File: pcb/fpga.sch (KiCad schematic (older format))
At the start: 29 parts, among them J1 CONN_INTEGRALSTICK_FPGA_DEVICE, Q1 SSM6N58NU, Q2 SSM6N58NU, Q3 SSM6N58NU, U12 DSC6001HI2A-025.0000‎, U2 XC7A50T-1FTG256C, U9 AT24MAC402-UDFN

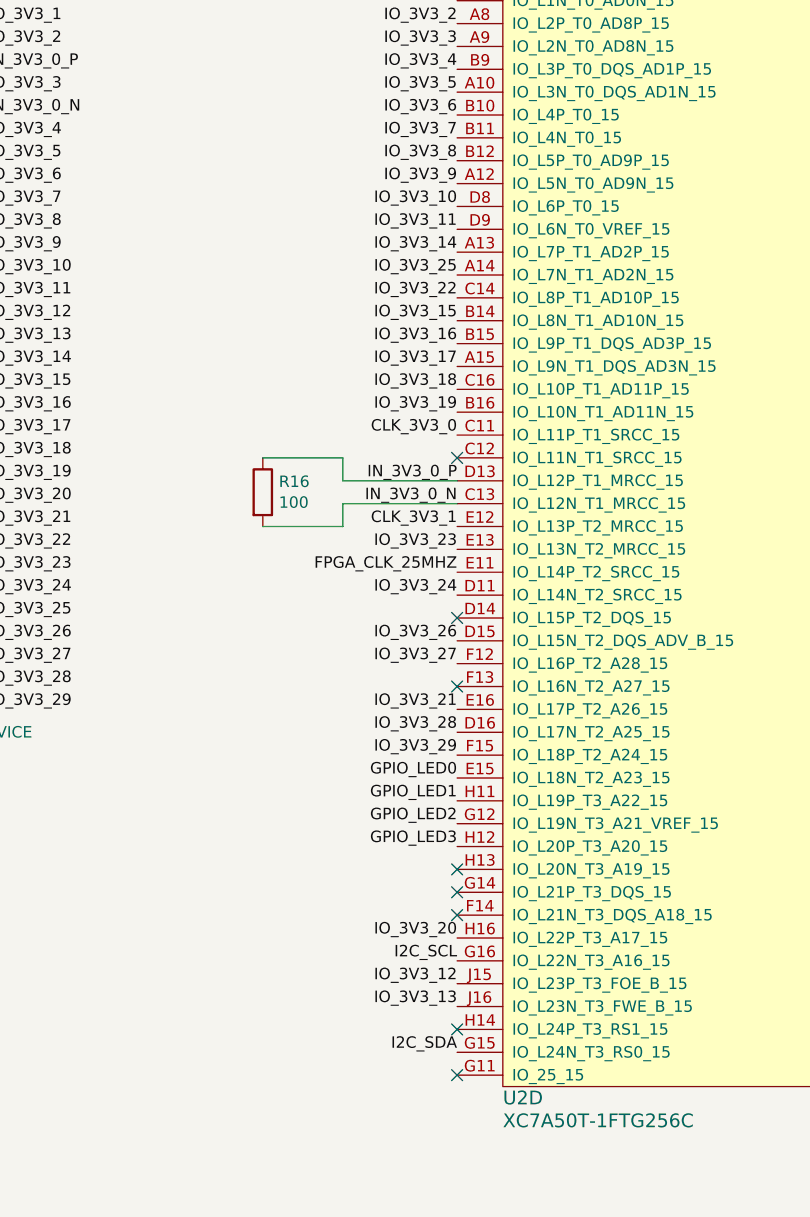
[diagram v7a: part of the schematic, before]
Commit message: Lots more routing of 3.3V GPIO bus
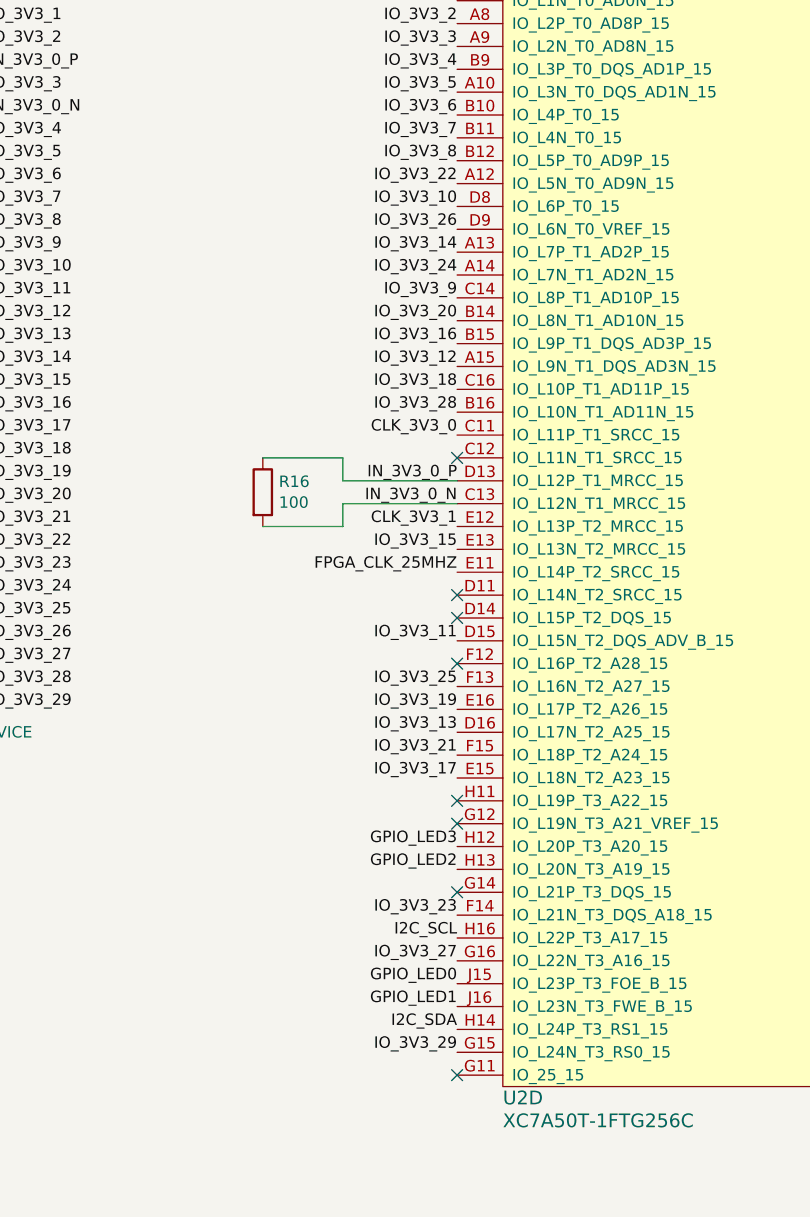
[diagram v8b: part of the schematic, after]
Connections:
- net GPIO_LED0: now also U2.J15 (IO_L23P_T3_FOE_B_15); no longer U2.E15 (IO_L18N_T2_A23_15)
- net GPIO_LED1: now also U2.J16 (IO_L23N_T3_FWE_B_15); no longer U2.H11 (IO_L19P_T3_A22_15)
- net GPIO_LED2: now also U2.H13 (IO_L20N_T3_A19_15); no longer U2.G12 (IO_L19N_T3_A21_VREF_15)
- net I2C_SCL: now also U2.H16 (IO_L22P_T3_A17_15); no longer U2.G16 (IO_L22N_T3_A16_15)
- net I2C_SDA: now also U2.H14 (IO_L24P_T3_RS1_15); no longer U2.G15 (IO_L24N_T3_RS0_15)
- net IO_3V3_11: now also U2.D15 (IO_L15N_T2_DQS_ADV_B_15); no longer U2.D9 (IO_L6N_T0_VREF_15)
- net IO_3V3_12: now also U2.A15 (IO_L9N_T1_DQS_AD3N_15); no longer U2.J15 (IO_L23P_T3_FOE_B_15)
- net IO_3V3_13: now also U2.D16 (IO_L17N_T2_A25_15); no longer U2.J16 (IO_L23N_T3_FWE_B_15)
- net IO_3V3_15: now also U2.E13 (IO_L13N_T2_MRCC_15); no longer U2.B14 (IO_L8N_T1_AD10N_15)
- net IO_3V3_17: now also U2.E15 (IO_L18N_T2_A23_15); no longer U2.A15 (IO_L9N_T1_DQS_AD3N_15)
- net IO_3V3_19: now also U2.E16 (IO_L17P_T2_A26_15); no longer U2.B16 (IO_L10N_T1_AD11N_15)
- net IO_3V3_20: now also U2.B14 (IO_L8N_T1_AD10N_15); no longer U2.H16 (IO_L22P_T3_A17_15)
- net IO_3V3_21: now also U2.F15 (IO_L18P_T2_A24_15); no longer U2.E16 (IO_L17P_T2_A26_15)
- net IO_3V3_22: now also U2.A12 (IO_L5N_T0_AD9N_15); no longer U2.C14 (IO_L8P_T1_AD10P_15)
- net IO_3V3_23: now also U2.F14 (IO_L21N_T3_DQS_A18_15); no longer U2.E13 (IO_L13N_T2_MRCC_15)
- net IO_3V3_24: now also U2.A14 (IO_L7N_T1_AD2N_15); no longer U2.D11 (IO_L14N_T2_SRCC_15)
- net IO_3V3_25: now also U2.F13 (IO_L16N_T2_A27_15); no longer U2.A14 (IO_L7N_T1_AD2N_15)
- net IO_3V3_26: now also U2.D9 (IO_L6N_T0_VREF_15); no longer U2.D15 (IO_L15N_T2_DQS_ADV_B_15)
- net IO_3V3_27: now also U2.G16 (IO_L22N_T3_A16_15); no longer U2.F12 (IO_L16P_T2_A28_15)
- net IO_3V3_28: now also U2.B16 (IO_L10N_T1_AD11N_15); no longer U2.D16 (IO_L17N_T2_A25_15)
- net IO_3V3_29: now also U2.G15 (IO_L24N_T3_RS0_15); no longer U2.F15 (IO_L18P_T2_A24_15)
- net IO_3V3_9: now also U2.C14 (IO_L8P_T1_AD10P_15); no longer U2.A12 (IO_L5N_T0_AD9N_15)
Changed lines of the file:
@@
 Sheet 6 8
 Title "INTEGRALSTICK Compute Module"
-Date "2018-11-11"
+Date "2018-11-12"
 Rev "0.1"
 Comp "Andrew D. Zonenberg"
@@
 Text Label 8400 1650 2    50   ~ 0
 IO_3V3_8
-Text Label 8400 1750 2    50   ~ 0
+Text Label 8400 2250 2    50   ~ 0
 IO_3V3_9
 Text Label 8400 1850 2    50   ~ 0
 IO_3V3_10
-Text Label 8400 1950 2    50   ~ 0
+Text Label 8400 3750 2    50   ~ 0
 IO_3V3_11
-Text Label 8400 5250 2    50   ~ 0
+Text Label 8400 2550 2    50   ~ 0
 IO_3V3_12
-Text Label 8400 5350 2    50   ~ 0
+Text Label 8400 4150 2    50   ~ 0
 IO_3V3_13
 Text Label 8400 2050 2    50   ~ 0
 IO_3V3_14
-Text Label 8400 2350 2    50   ~ 0
+Text Label 8400 3350 2    50   ~ 0
 IO_3V3_15
 Text Label 8400 2450 2    50   ~ 0
 IO_3V3_16
-Text Label 8400 2550 2    50   ~ 0
+Text Label 8400 4350 2    50   ~ 0
 IO_3V3_17
 Text Label 8400 2650 2    50   ~ 0
 IO_3V3_18
+Text Label 8400 4050 2    50   ~ 0
+IO_3V3_19
+Text Label 8400 2350 2    50   ~ 0
+IO_3V3_20
+Text Label 8400 4250 2    50   ~ 0
+IO_3V3_21
+Text Label 8400 1750 2    50   ~ 0
+IO_3V3_22
+Text Label 8400 4950 2    50   ~ 0
+IO_3V3_23
+Text Label 8400 2150 2    50   ~ 0
+IO_3V3_24
+Text Label 8400 3950 2    50   ~ 0
+IO_3V3_25
+Text Label 8400 1950 2    50   ~ 0
+IO_3V3_26
+Text Label 8400 5150 2    50   ~ 0
+IO_3V3_27
 Text Label 8400 2750 2    50   ~ 0
-IO_3V3_19
-Text Label 8400 5050 2    50   ~ 0
-IO_3V3_20
-Text Label 8400 4050 2    50   ~ 0
-IO_3V3_21
-Text Label 8400 2250 2    50   ~ 0
-IO_3V3_22
-Text Label 8400 3350 2    50   ~ 0
-IO_3V3_23
-Text Label 8400 3550 2    50   ~ 0
-IO_3V3_24
-Text Label 8400 2150 2    50   ~ 0
-IO_3V3_25
-Text Label 8400 3750 2    50   ~ 0
-IO_3V3_26
-Text Label 8400 3850 2    50   ~ 0
-IO_3V3_27
-Text Label 8400 4150 2    50   ~ 0
 IO_3V3_28
-Text Label 8400 4250 2    50   ~ 0
+Text Label 8400 5550 2    50   ~ 0
 IO_3V3_29
 Text Label 8400 3050 2    50   ~ 0
@@
 Text Label 8400 3150 2    50   ~ 0
 IN_3V3_0_N
-NoConn ~ 8400 4750
 NoConn ~ 8400 4850
-NoConn ~ 8400 4950
 NoConn ~ 8400 5650
 $Comp
@@
 Wire Wire Line
 	5000 7850 5350 7850
-Text Label 8400 5150 2    50   ~ 0
+Text Label 8400 5050 2    50   ~ 0
 I2C_SCL
-Text Label 8400 5550 2    50   ~ 0
+Text Label 8400 5450 2    50   ~ 0
 I2C_SDA
 $Comp
@@
 Wire Wire Line
 	8150 9450 9300 9450
-Text Label 8400 4350 2    50   ~ 0
+Text Label 8400 5250 2    50   ~ 0
 GPIO_LED0
-Text Label 8400 4450 2    50   ~ 0
+Text Label 8400 5350 2    50   ~ 0
 GPIO_LED1
-Text Label 8400 4550 2    50   ~ 0
+Text Label 8400 4750 2    50   ~ 0
 GPIO_LED2
 Text Label 8400 4650 2    50   ~ 0
@@
 Wire Wire Line
 	13650 4350 13900 4350
-NoConn ~ 8400 5450
-NoConn ~ 8400 3950
 NoConn ~ 8400 3650
 $Comp
@@
 Text Notes 900  4000 0    50   ~ 0
 LVDS_DQ3 polarity swapped for routability
+NoConn ~ 8400 3850
+NoConn ~ 8400 3550
+NoConn ~ 8400 4550
+NoConn ~ 8400 4450
 $EndSCHEMATC
